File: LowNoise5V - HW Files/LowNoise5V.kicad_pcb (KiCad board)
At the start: 2 copper layers, 8 parts, among them J1 USB_A

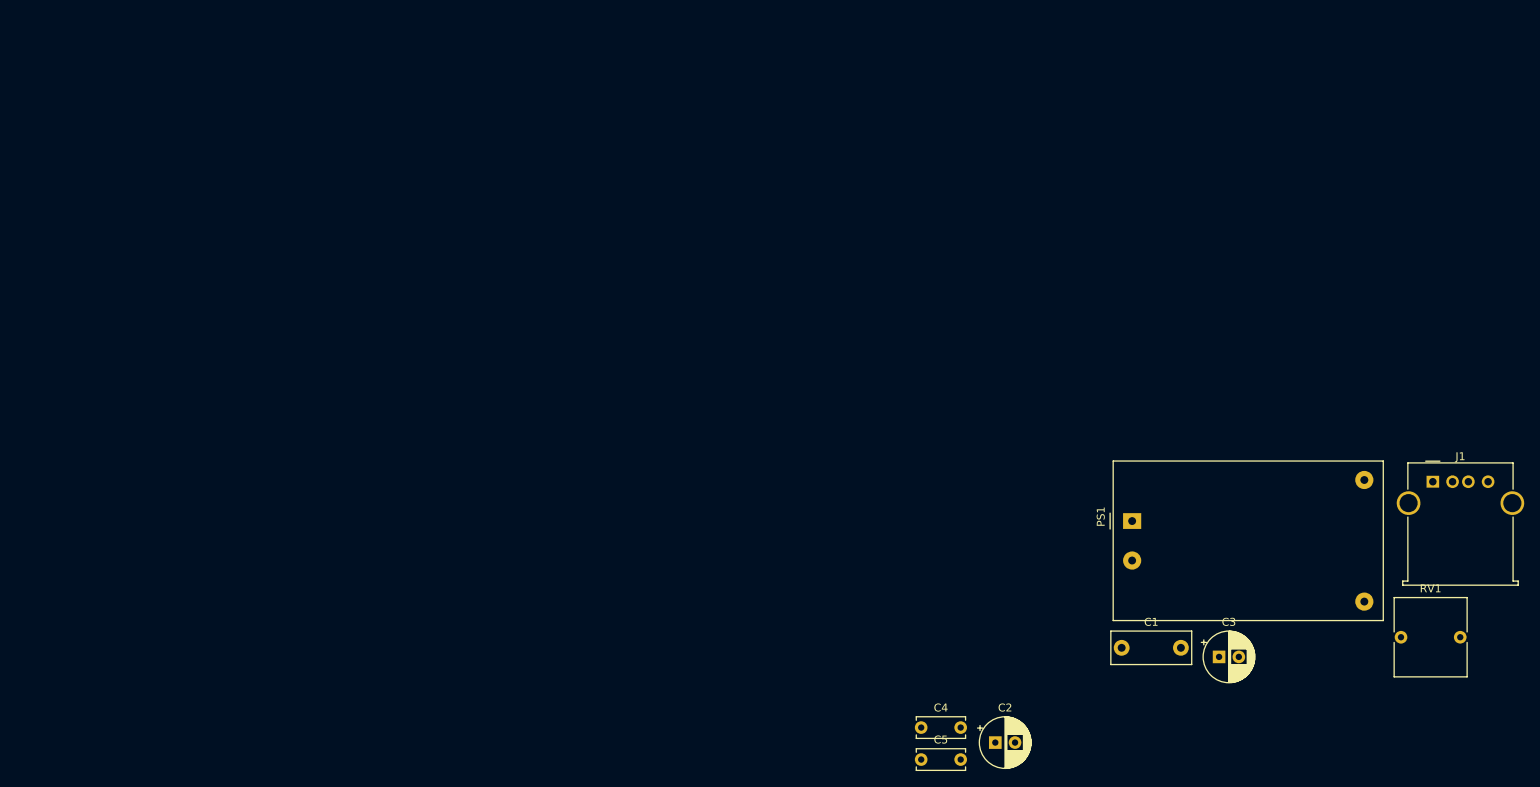
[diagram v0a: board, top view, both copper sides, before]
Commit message: Customize footprints and place more components
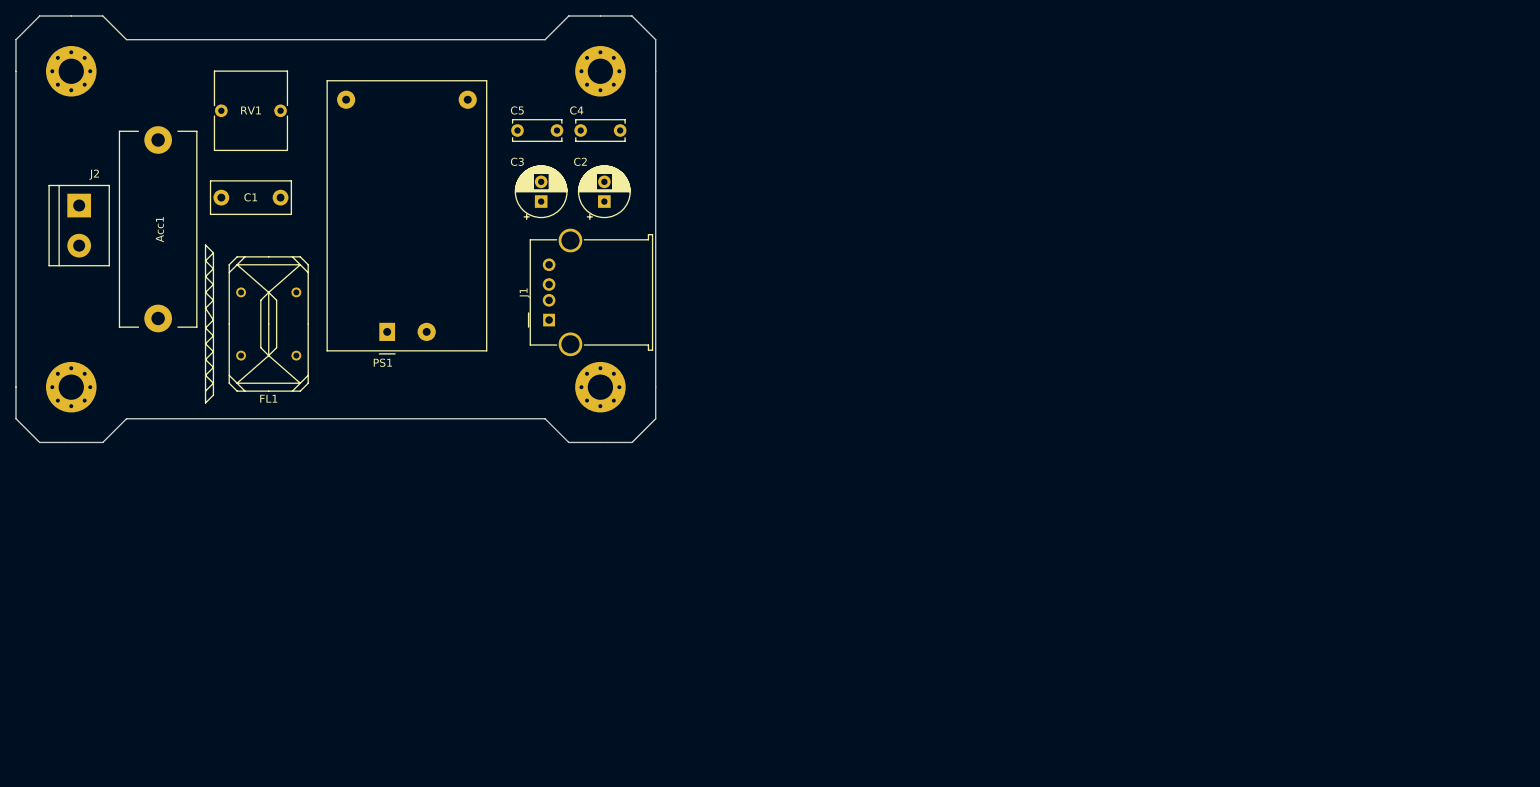
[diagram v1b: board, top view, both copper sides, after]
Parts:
- added Acc1: Fuse Holder, LowNoise5V:FuseHolder, F.Cu at (18.0, 27.0)
- added FL1: Power Line 10mH @ 1kHz 1.2Ω, LowNoise5V:EMI Choke, F.Cu at (32.0, 39.0)
- added J2: Conn_01x02, TerminalBlock:TerminalBlock_bornier-2_P5.08mm, F.Cu at (8.00, 24.0)
- added REF**: MountingHole_3.2mm_M3_Pad_Via, MountingHole:MountingHole_3.2mm_M3_Pad_Via, F.Cu at (74.0, 7.00)
- added REF**: MountingHole_3.2mm_M3_Pad_Via, MountingHole:MountingHole_3.2mm_M3_Pad_Via, F.Cu at (74.0, 47.0)
- added REF**: MountingHole_3.2mm_M3_Pad_Via, MountingHole:MountingHole_3.2mm_M3_Pad_Via, F.Cu at (7.00, 47.0)
- added REF**: MountingHole_3.2mm_M3_Pad_Via, MountingHole:MountingHole_3.2mm_M3_Pad_Via, F.Cu at (7.00, 7.00)
- J1: footprint Connector_USB:USB_A_Molex_67643_Horizontal -> LowNoise5V:USB_A_Molex_67643_Horizontal
- PS1: footprint Converter_ACDC:Converter_ACDC_HiLink_HLK-PMxx -> LowNoise5V:Converter_ACDC_HiLink_HLK-PMxx
- moved RV1 163.6 mm to (26.0, 12.0)
- moved C1 127.5 mm to (26.0, 23.0)
- moved J1 113.8 mm to (67.5, 38.5), turned to 90 degrees
- moved C3 103.4 mm to (66.5, 23.5), turned to 90 degrees
- moved PS1 97.3 mm to (47.0, 40.0), turned to 90 degrees
- moved C5 94.6 mm to (63.5, 14.5)
- moved C4 87.0 mm to (71.5, 14.5)
- moved C2 84.5 mm to (74.5, 23.5), turned to 90 degrees
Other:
- board outline added: 81 x 54 mm

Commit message: move around components
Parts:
- moved C4 25.9 mm to (63.0, 39.0)
- moved C5 25.9 mm to (72.0, 39.0)
- moved C2 8.06 mm to (75.5, 15.5)
- moved C3 8.06 mm to (67.5, 15.5)
- moved J1 7.65 mm to (69.0, 31.0)

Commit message: Finalize Routing
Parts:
- removed Acc1: Fuse Holder, LowNoise5V:FuseHolder
- added F1: 500mA 250VAC Fast Blow, LowNoise5V:FuseHolder, F.Cu at (18.2, 27.0)
- J2: footprint TerminalBlock:TerminalBlock_bornier-2_P5.08mm -> LowNoise5V:1935161
- moved J2 3.16 mm to (7.00, 27.0), turned to 90 degrees
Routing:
- net AC_Neutral: track 0.00 -> 57.9 mm
- net Net-(C1-Pad1): track 0.00 -> 35.7 mm
- net Net-(FL1-Pad3): track 0.00 -> 24.0 mm
- net AC_Line: track 0.00 -> 22.3 mm
- net Net-(FL1-Pad2): track 0.00 -> 13.6 mm
- added copper zone on B.Cu, net +5V
- added copper zone on F.Cu, net GND
